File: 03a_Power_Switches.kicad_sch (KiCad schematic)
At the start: 28 parts, among them U10 TPS20xxC, U12 TPS20xxC, U14 TPS20xxC, U9 TPS20xxC

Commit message: fix symbols, route UFP DPs and voltage regs
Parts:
- R27, R28, R29, R30: footprint Resistor_SMD:R_0603_1608Metric -> Resistor_SMD:R_0402_1005Metric
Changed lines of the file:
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@@
       (effects (font (size 1.27 1.27)))
     )
-    (property "Footprint" "Resistor_SMD:R_0603_1608Metric" (at 77.47 55.118 90)
+    (property "Footprint" "Resistor_SMD:R_0402_1005Metric" (at 77.47 55.118 90)
       (effects (font (size 1.27 1.27)) hide)
     )
@@
       (effects (font (size 1.27 1.27)))
     )
-    (property "Footprint" "Resistor_SMD:R_0603_1608Metric" (at 77.47 86.868 90)
+    (property "Footprint" "Resistor_SMD:R_0402_1005Metric" (at 77.47 86.868 90)
       (effects (font (size 1.27 1.27)) hide)
     )
@@
       (effects (font (size 1.27 1.27)))
     )
-    (property "Footprint" "Resistor_SMD:R_0603_1608Metric" (at 77.47 140.208 90)
+    (property "Footprint" "Resistor_SMD:R_0402_1005Metric" (at 77.47 140.208 90)
       (effects (font (size 1.27 1.27)) hide)
     )
@@
       (effects (font (size 1.27 1.27)))
     )
-    (property "Footprint" "Resistor_SMD:R_0603_1608Metric" (at 77.47 113.538 90)
-      (effects (font (size 1.27 1.27)) hide)
-    )
+    (property "Footprint" "Resistor_SMD:R_0402_1005Metric" (at 77.47 113.538 90)
+      (effects (font (size 1.27 1.27)) hide)
+    )

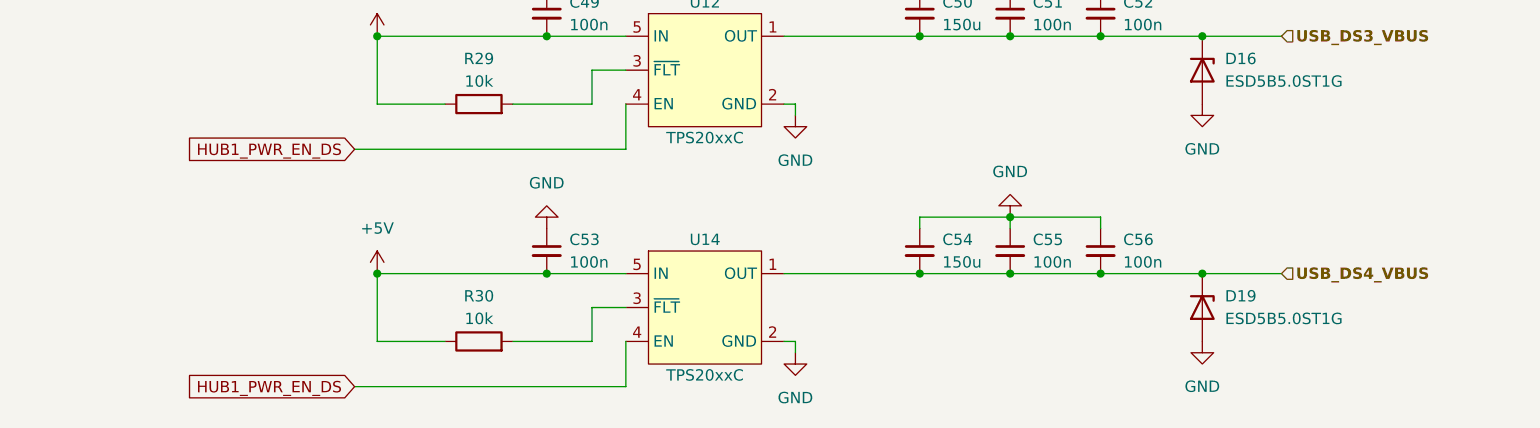
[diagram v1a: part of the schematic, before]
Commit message: add RTL8153
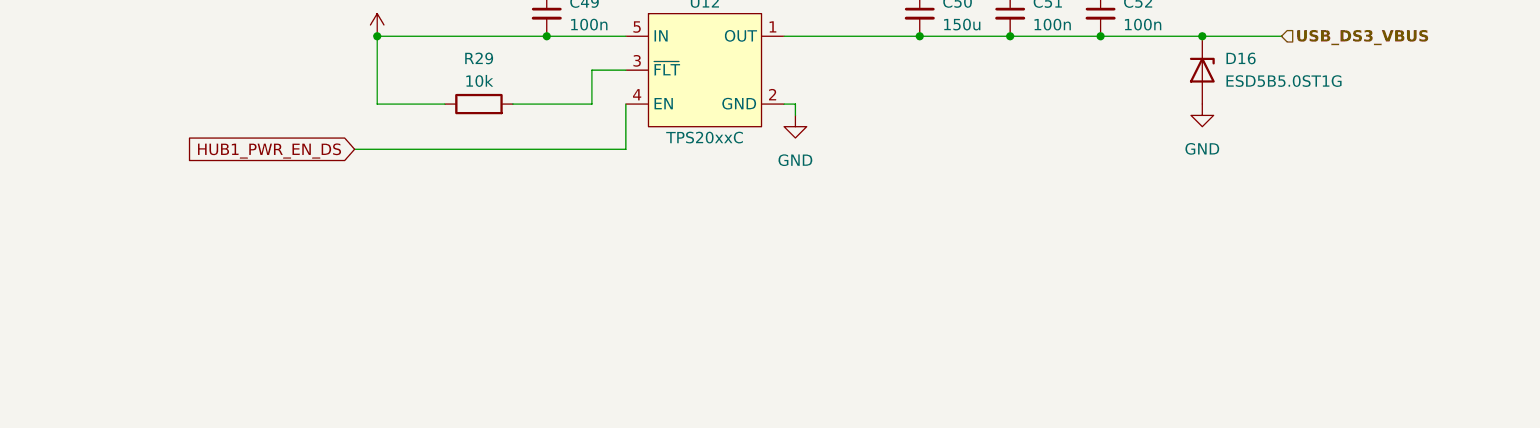
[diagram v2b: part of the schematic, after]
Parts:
- removed C53, C55, C56: 100n, Capacitor_SMD:C_0603_1608Metric, symbol Device:C_Small
- removed C54: 150u, Capacitor_SMD:C_Elec_6.3x7.7, symbol Device:C_Small
- removed D19: ESD5B5.0ST1G, Diode_SMD:D_SOD-523, symbol Device:D_Zener
- removed R30: 10k, Resistor_SMD:R_0402_1005Metric, symbol Device:R
- removed U14: TPS20xxC, Package_TO_SOT_SMD:SOT-23-5, symbol CakeUSB:TPS20xxC

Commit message: route power delivery controller
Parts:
- renumbered C41 to C114, C42 to C115, C43 to C116, C44 to C117, C45 to C118, C46 to C119, C47 to C120, C48 to C121, C49 to C122, C50 to C123, C51 to C124, C52 to C125, D11 to D15, D15 to D16, D16 to D17, R27 to R38, R28 to R39, R29 to R40, U9 to U12, U10 to U13, U12 to U14
